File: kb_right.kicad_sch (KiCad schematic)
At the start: 181 parts, among them J1 10029449-001RLF, J2 Conn_01x06, J3 Conn_01x06, J4 Conn_01x06, J5 Conn_01x06, SW1 RotaryEncoder_Switch

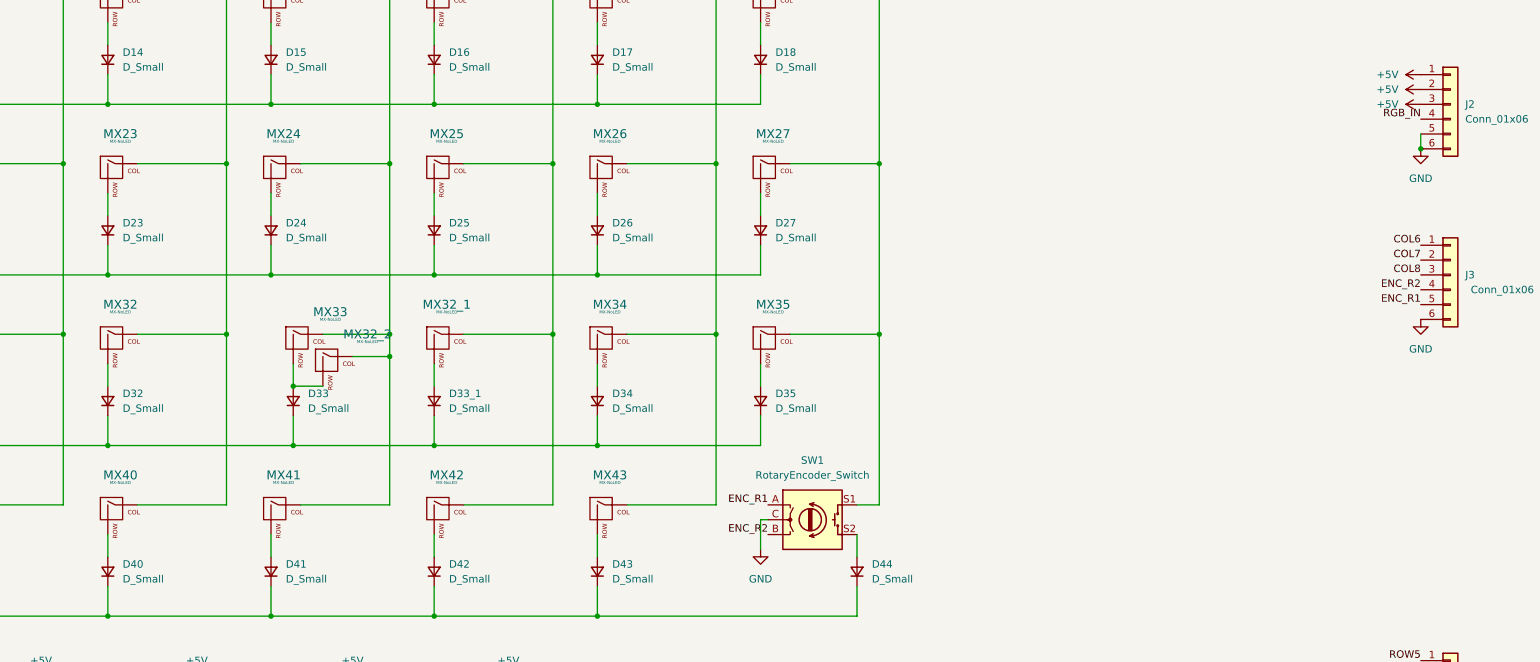
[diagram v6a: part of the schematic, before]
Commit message: add via stitching
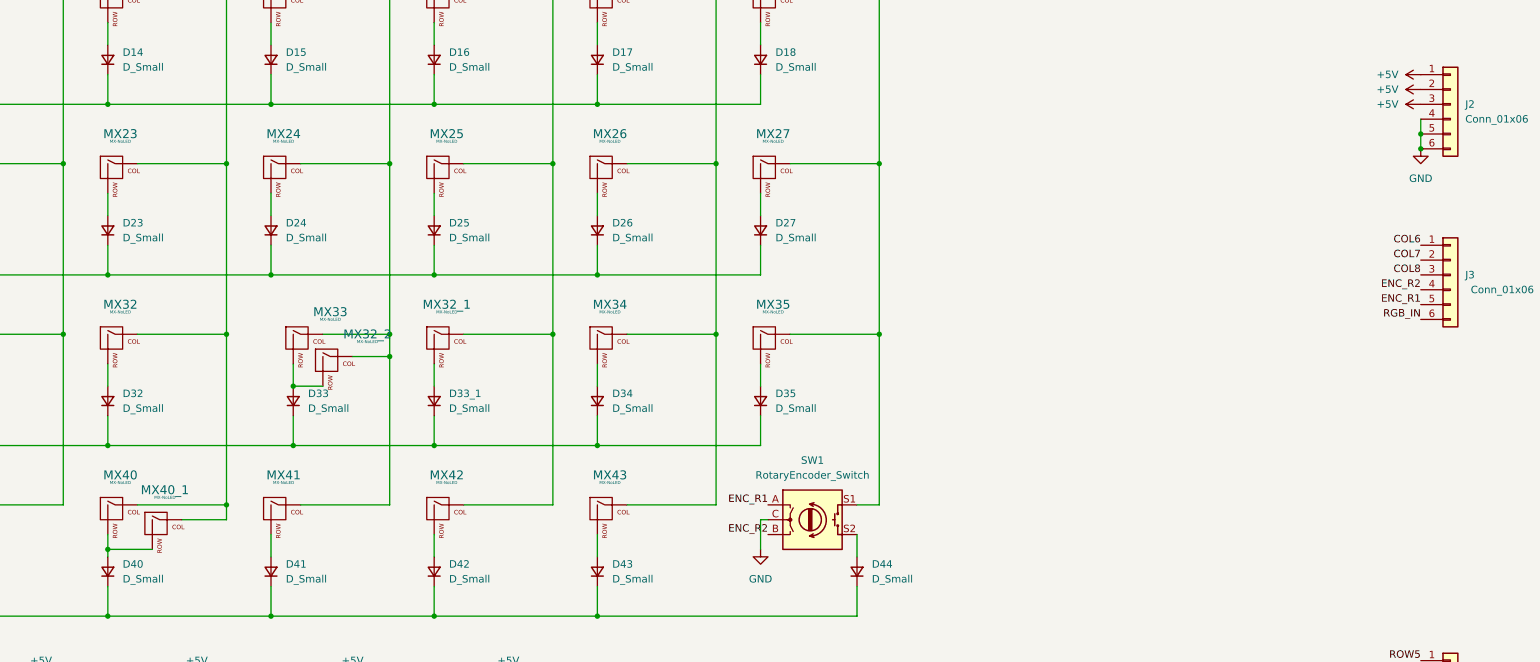
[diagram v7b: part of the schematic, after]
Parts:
- added MX40_1: MX-NoLED, MX_Only:MXOnly-1.5U-Hotswap, symbol MX_Alps_Hybrid:MX-NoLED
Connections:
- net COL4: now also MX40_1.1 (COL)
- net GND: now also J2.4 (Pin_4); no longer J3.6 (Pin_6)
- net RGB_IN: now also J3.6 (Pin_6); no longer J2.4 (Pin_4)
- net at D40.2 (A), MX40.2 (ROW): now also MX40_1.2 (ROW)
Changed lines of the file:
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@@
   (junction (at 255.27 214.63) (diameter 0) (color 0 0 0 0)
   )
+  (junction (at 160.02 157.48) (diameter 0) (color 0 0 0 0)
+  )
   (junction (at 215.9 168.91) (diameter 0) (color 0 0 0 0)
   )
@@
   (junction (at 97.79 91.44) (diameter 0) (color 0 0 0 0)
   )
+  (junction (at 180.34 149.86) (diameter 0) (color 0 0 0 0)
+  )
   (junction (at 77.47 168.91) (diameter 0) (color 0 0 0 0)
   )
@@
   (junction (at 68.58 229.87) (diameter 0) (color 0 0 0 0)
   )
+  (junction (at 384.81 86.36) (diameter 0) (color 0 0 0 0)
+  )
   (junction (at 243.84 110.49) (diameter 0) (color 0 0 0 0)
   )
@@
     (stroke (width 0) (type default) (color 0 0 0 0))
   )
+  (wire (pts (xy 160.02 157.48) (xy 167.64 157.48))
+    (stroke (width 0) (type default) (color 0 0 0 0))
+  )
   (wire (pts (xy 54.61 62.23) (xy 69.85 62.23))
     (stroke (width 0) (type default) (color 0 0 0 0))
@@
     (stroke (width 0) (type default) (color 0 0 0 0))
   )
-  (wire (pts (xy 160.02 154.94) (xy 160.02 158.75))
+  (wire (pts (xy 160.02 154.94) (xy 160.02 157.48))
     (stroke (width 0) (type default) (color 0 0 0 0))
   )
@@
     (stroke (width 0) (type default) (color 0 0 0 0))
   )
+  (wire (pts (xy 172.72 152.4) (xy 180.34 152.4))
+    (stroke (width 0) (type default) (color 0 0 0 0))
+  )
   (wire (pts (xy 68.58 293.37) (xy 58.42 293.37))
     (stroke (width 0) (type default) (color 0 0 0 0))
@@
     (stroke (width 0) (type default) (color 0 0 0 0))
   )
+  (wire (pts (xy 160.02 157.48) (xy 160.02 158.75))
+    (stroke (width 0) (type default) (color 0 0 0 0))
+  )
   (wire (pts (xy 85.09 278.13) (xy 95.25 278.13))
     (stroke (width 0) (type default) (color 0 0 0 0))
@@
     (stroke (width 0) (type default) (color 0 0 0 0))
   )
+  (wire (pts (xy 384.81 83.82) (xy 384.81 86.36))
+    (stroke (width 0) (type default) (color 0 0 0 0))
+  )
   (wire (pts (xy 191.77 125.73) (xy 191.77 129.54))
     (stroke (width 0) (type default) (color 0 0 0 0))
@@
     (stroke (width 0) (type default) (color 0 0 0 0))
   )
+  (wire (pts (xy 180.34 152.4) (xy 180.34 149.86))
+    (stroke (width 0) (type default) (color 0 0 0 0))
+  )
   (wire (pts (xy 165.1 120.65) (xy 180.34 120.65))
     (stroke (width 0) (type default) (color 0 0 0 0))
@@
     (effects (font (size 1.27 1.27)) (justify left bottom))
   )
+  (label "RGB_IN" (at 384.81 118.11 180)
+    (effects (font (size 1.27 1.27)) (justify right bottom))
+  )
   (label "COL1" (at 397.51 25.4 0)
     (effects (font (size 1.27 1.27)) (justify left bottom))
@@
     (effects (font (size 1.27 1.27)) (justify right bottom))
   )
-  (label "RGB_IN" (at 384.81 83.82 180)
-    (effects (font (size 1.27 1.27)) (justify right bottom))
-  )
   (label "COL2" (at 416.56 181.61 180)
     (effects (font (size 1.27 1.27)) (justify right bottom))
@@
     (pin "1")
   )
-  (symbol (lib_id "power:GND") (at 384.81 118.11 0) (unit 1)
-    (in_bom yes) (on_board yes) (fields_autoplaced)
-    (property "Reference" "#PWR06" (id 0) (at 384.81 124.46 0)
-      (effects (font (size 1.27 1.27)) hide)
-    )
-    (property "Value" "GND" (id 1) (at 384.81 123.19 0))
-    (property "Footprint" "" (id 2) (at 384.81 118.11 0)
-      (effects (font (size 1.27 1.27)) hide)
-    )
-    (property "Datasheet" "" (id 3) (at 384.81 118.11 0)
-      (effects (font (size 1.27 1.27)) hide)
-    )
-    (pin "1")
-  )
   (symbol (lib_id "Device:D_Small") (at 191.77 132.08 90) (unit 1)
     (in_bom yes) (on_board yes) (fields_autoplaced)
@@
     (pin "2")
   )
+  (symbol (lib_id "MX_Alps_Hybrid:MX-NoLED") (at 168.91 153.67 0) (unit 1)
+    (in_bom yes) (on_board yes) (fields_autoplaced)
+    (property "Reference" "MX40_1" (id 0) (at 169.7956 147.32 0)
+      (effects (font (size 1.524 1.524)))
+    )
+    (property "Value" "MX-NoLED" (id 1) (at 169.7956 148.59 0)
+      (effects (font (size 0.508 0.508)))
+    )
+    (property "Footprint" "MX_Only:MXOnly-1.5U-Hotswap" (id 2) (at 153.035 154.305 0)
+      (effects (font (size 1.524 1.524)) hide)
+    )
+    (property "Datasheet" "" (id 3) (at 153.035 154.305 0)
+      (effects (font (size 1.524 1.524)) hide)
+    )
+    (pin "1")
+    (pin "2")
+  )
   (symbol (lib_id "MX_Alps_Hybrid:MX-NoLED") (at 275.59 34.29 0) (unit 1)
     (in_bom yes) (on_board yes) (fields_autoplaced)
@@
       (reference "#PWR05") (unit 1) (value "GND") (footprint "")
     )
-    (path "/9eb87353-05db-464a-8737-3996a6b1426c"
-      (reference "#PWR06") (unit 1) (value "GND") (footprint "")
-    )
     (path "/63b71a88-d9fd-4c7e-80e7-c959cbee7ec9"
       (reference "#PWR07") (unit 1) (value "GND") (footprint "")
@@
       (reference "MX40") (unit 1) (value "MX-NoLED") (footprint "MX_Only:MXOnly-1.25U-Hotswap")
     )
+    (path "/ce79a304-68f0-451c-bdd5-4efb1f96e84a"
+      (reference "MX40_1") (unit 1) (value "MX-NoLED") (footprint "MX_Only:MXOnly-1.5U-Hotswap")
+    )
     (path "/ad50f95c-84e1-49c5-a642-ec625b8d7790"

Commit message: add sideways encoder
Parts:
- removed J3, J5: Conn_01x06, Connector_PinHeader_2.54mm:PinHeader_1x06_P2.54mm_Vertical, symbol Connector_Generic:Conn_01x06
- added SW2: RotaryEncoder, Keebio-Parts:RotaryEncoder_EC11B-Horizontal-No-Pushbutton, symbol Device:RotaryEncoder
- J2: value Conn_01x06 -> Conn_02x06_Odd_Even; footprint Connector_PinHeader_2.54mm:PinHeader_1x06_P2.54mm_Vertical -> Connector_PinHeader_2.54mm:PinHeader_2x06_P2.54mm_Vertical; symbol Connector_Generic:Conn_01x06 -> Connector_Generic:Conn_02x06_Odd_Even
- J3: renamed from J4; value Conn_01x06 -> Conn_02x06_Odd_Even; footprint Connector_PinHeader_2.54mm:PinHeader_1x06_P2.54mm_Vertical -> Connector_PinHeader_2.54mm:PinHeader_2x06_P2.54mm_Vertical; symbol Connector_Generic:Conn_01x06 -> Connector_Generic:Conn_02x06_Odd_Even
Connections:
- net +5V: now also J2.5 (Pin_5); no longer J2.2 (Pin_2)
- net COL0: now also J3.2 (Pin_2)
- net COL1: now also J3.4 (Pin_4)
- net COL2: now also J3.6 (Pin_6)
- net COL3: now also J3.8 (Pin_8)
- net COL4: now also J3.10 (Pin_10)
- net COL5: now also J3.12 (Pin_12)
- net COL6: now also J2.2 (Pin_2)
- net COL7: now also J2.4 (Pin_4)
- net COL8: now also J2.6 (Pin_6)
- net ENC_R1: now also J2.10 (Pin_10), SW2.A
- net ENC_R2: now also J2.8 (Pin_8), SW2.B
- net GND: now also J2.11 (Pin_11), J2.7 (Pin_7), J2.9 (Pin_9), J3.11 (Pin_11), SW2.C; no longer J2.4 (Pin_4), J2.5 (Pin_5), J2.6 (Pin_6), J3.6 (Pin_6)
- net RGB_IN: now also J2.12 (Pin_12)
- net ROW6: now also J3.3 (Pin_3); no longer J3.2 (Pin_2)
- net ROW7: now also J3.5 (Pin_5); no longer J3.3 (Pin_3)
- net ROW8: now also J3.7 (Pin_7); no longer J3.4 (Pin_4)
- net ROW9: now also J3.9 (Pin_9); no longer J3.5 (Pin_5)
